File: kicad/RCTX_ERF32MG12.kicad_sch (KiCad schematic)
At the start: 93 parts, among them J20 USB_OTG, P10 LEDs, P4 SWD, P6 SD Card, P9 BUZZ, SW2 RESET, U10 ATSAMD11D14A-M, U11 USB6B1

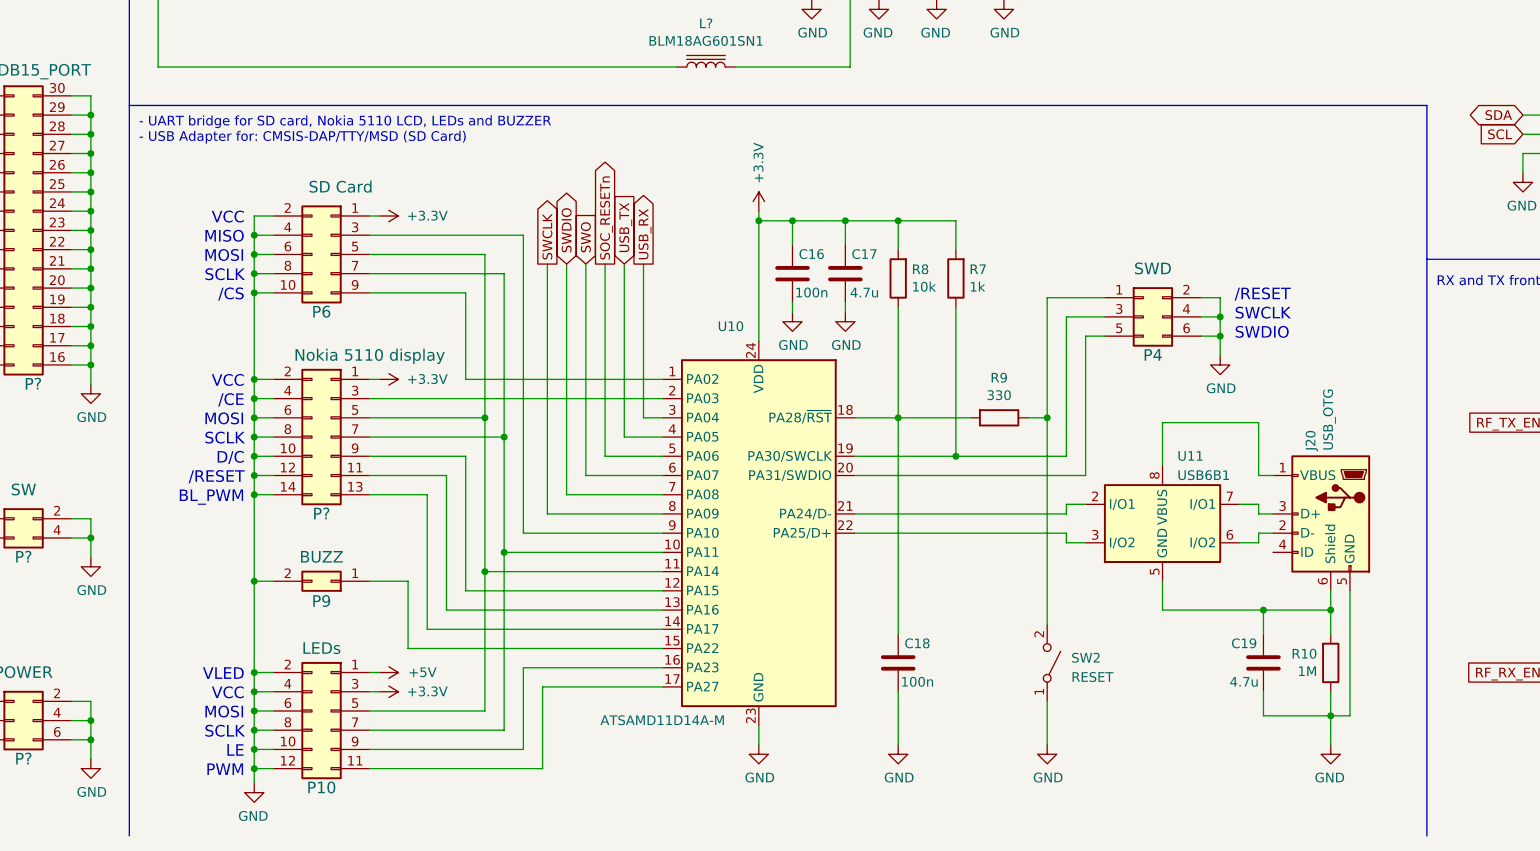
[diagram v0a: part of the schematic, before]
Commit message: Using SAMD11D14M instead of PIC16F1459 for USB bridge - updating schematics
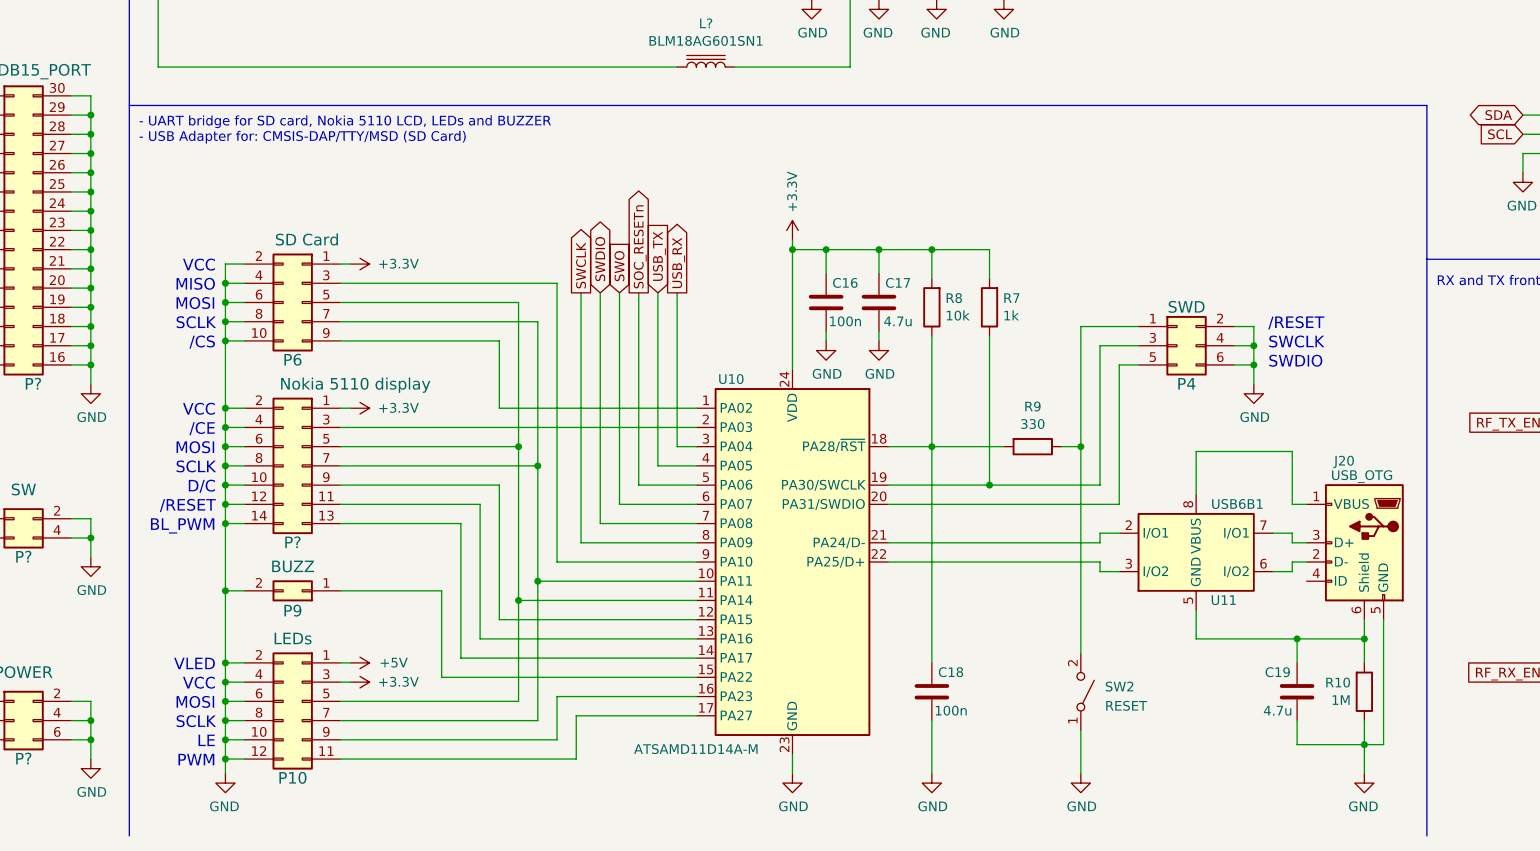
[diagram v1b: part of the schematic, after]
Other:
- moved on the sheet: C16, C17, C18, C19, J20, P10, P4, P6, P9, P?, R10, R7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

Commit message: Using SAMD11D14M instead of PIC16F1459 for USB bridge - updating schematics
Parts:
- removed C? (x6): 100p, symbol device:C
- removed P4: SWD, symbol conn:Conn_02x03_Odd_Even
- removed R8: 10k, symbol device:R
- removed R9: 330, symbol device:R
- removed SW2: RESET, symbol RCTX-rescue:SW_SPST-switches
- removed U? (x2): MAX2650, smd-semi:SOT-143, symbol RCTX_ERF32MG12-rescue:MAX2650-maxim_1
- added C1, C2, C20, C21, C22: 100p, symbol device:C
- added J21, J22: USB, symbol Connector_Generic:Conn_01x03
- added P?: AUX_DB9_PORT, symbol Connector_Generic:Conn_02x09_Odd_Even
- added U1, U12: MAX2650, smd-semi:SOT-143, symbol maxim_1:MAX2650
- C18: value 100n -> 100p
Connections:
- net +3V3: now also P?.3 (Pin_3)
- net +5V: now also P?.1 (Pin_1)
- net GND: now also C18.2, C20.2, J21.3 (Pin_3), J22.3 (Pin_3), P?.10 (Pin_10), P?.12 (Pin_12), P?.14 (Pin_14), P?.16 (Pin_16), P?.18 (Pin_18), P?.2 (Pin_2), P?.4 (Pin_4), P?.6 (Pin_6), P?.8 (Pin_8), U1.4 (VCC), U12.2 (GND); no longer C18.1
- net RF_RX_VCC: now also C20.1, U12.4 (VCC)
- net RF_TX_VCC: now also C18.1, U1.2 (GND)
- net SOC_RESETn: now also P?.5 (Pin_5)
- net at U?.8 (RF), U?.8 (RF): now also C21.2, C22.1
- net at U?.3 (RF1): now also C1.1, C2.2
- net at U11.2 (I/O1): now also J22.1 (Pin_1); no longer U10.21 (PA24/D-)
- net at U11.3 (I/O2): now also J22.2 (Pin_2); no longer U10.22 (PA25/D+)
- net DAP_SWCLK: now reaches R7.1, U10.19 (PA30/SWCLK)
- net DAP_SWCLK: now also P?.15 (Pin_15)
- net DAP_SWDIO: now reaches U10.20 (PA31/SWDIO)
- net DAP_SWDIO: now also P?.13 (Pin_13)
- net DAP_RESETn: now reaches U10.18 (PA28/~{RST})
- net DAP_RESETn: now also P?.17 (Pin_17); no longer C18.2
- net SWCLK renamed SOC_SWCLK
- net SOC_SWCLK: now also P?.11 (Pin_11)
- net SWDIO renamed SOC_SWDIO
- net SOC_SWDIO: now also P?.9 (Pin_9)
- net SWO renamed SOC_SWO
- net SOC_SWO: now also P?.7 (Pin_7)
- new net: C22.2, U12.1 (OUT)
- new net: C2.1, U12.3 (IN)
- new net: C21.1, U1.3 (IN)
- new net: J21.1 (Pin_1), U10.21 (PA24/D-)
- new net: J21.2 (Pin_2), U10.22 (PA25/D+)
- new net: C1.2, U1.1 (OUT)
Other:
- note added: "- Micro USB connector"
- note added: "HF/VHF band filter"
- note added: "Sub-GHz multiband 110 MHz up-down converter, pre-amp and power-amp RF MHz ± LO MHz -> IF MHz ------------------------ 10 ... 80 + 110 -> 120-190 430 ... 460 - 110 -> 320-350"
- note added: "UHF band filter"
- note removed: "110 MHz"
- note removed: "SWCLK"
- note removed: "SWDIO"
- moved on the sheet: C16, C17, C19, C?, J20, J?, L?, P10, P6, P9, P?, R10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

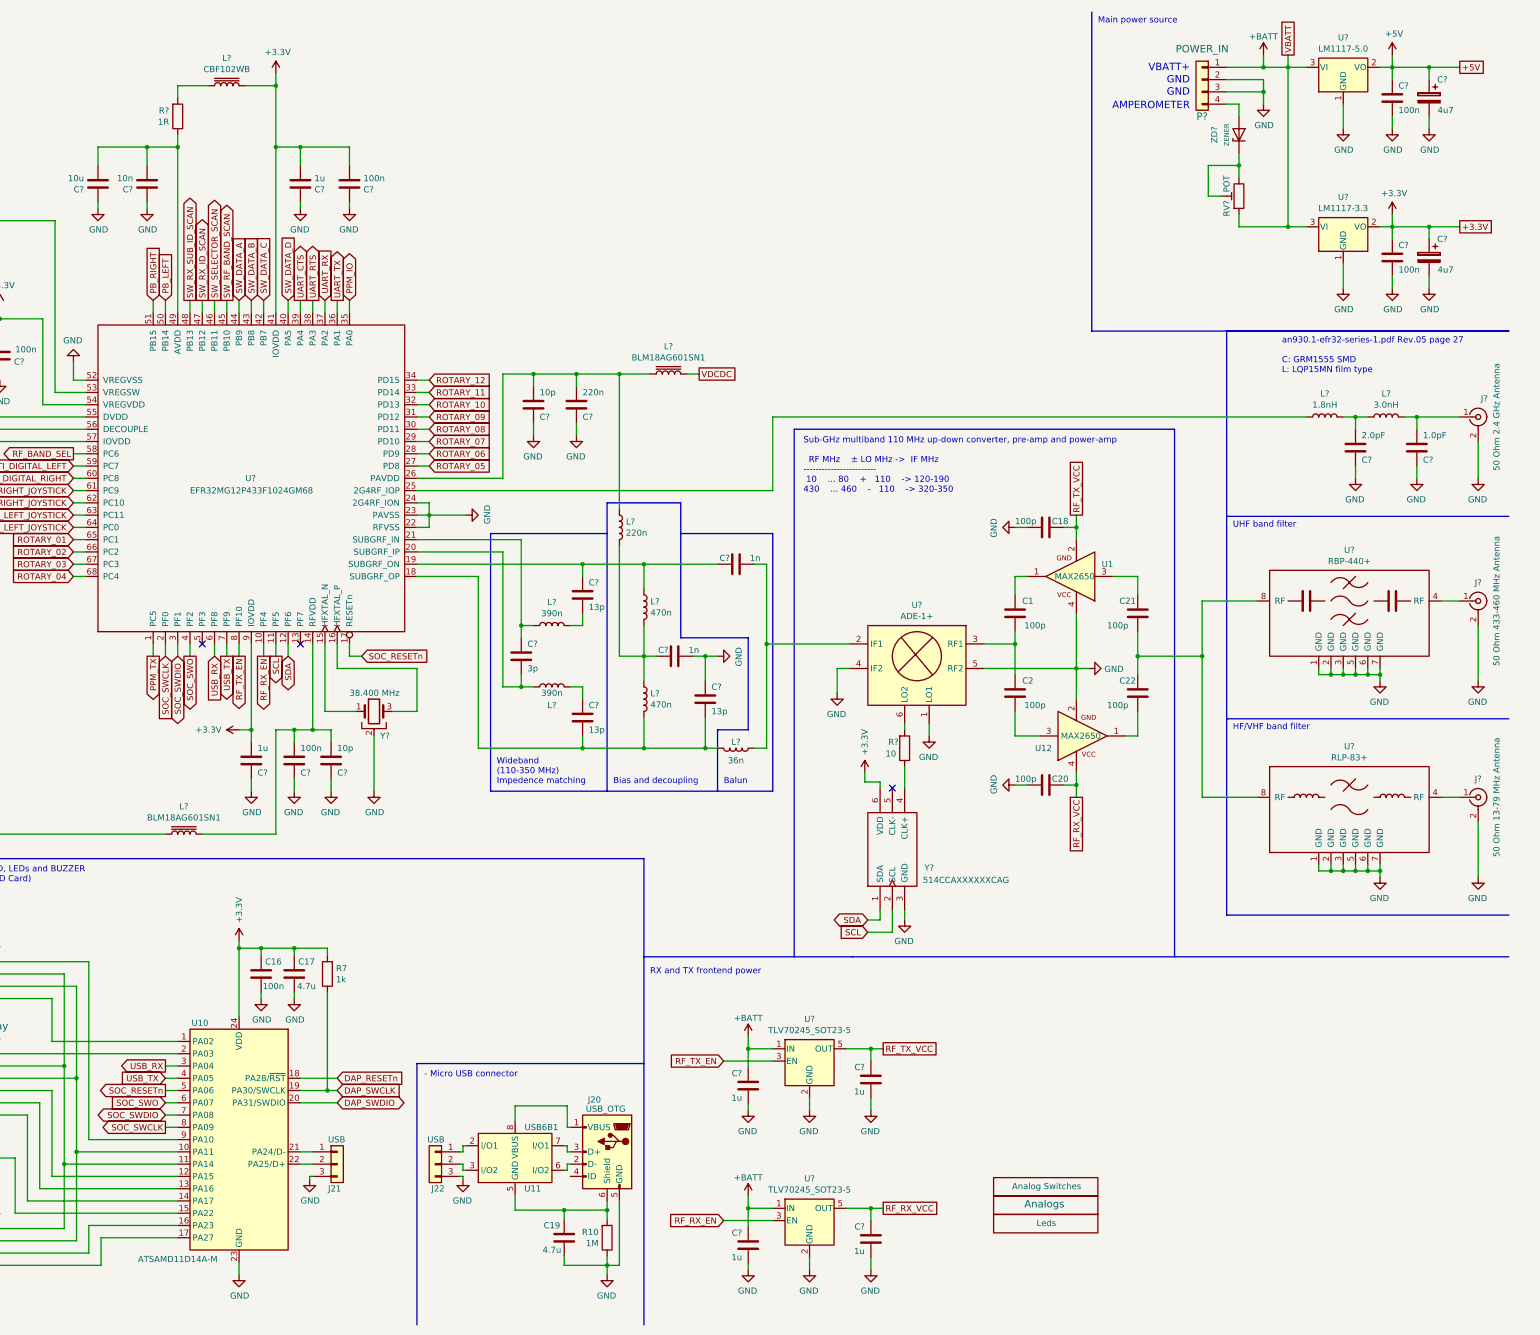
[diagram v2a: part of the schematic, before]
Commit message: Driving the EFR32 reset with the SAMD11 reset pin as GPIO to have an additional GPIO for the SPI {EFR32<->SAMD11} CLK
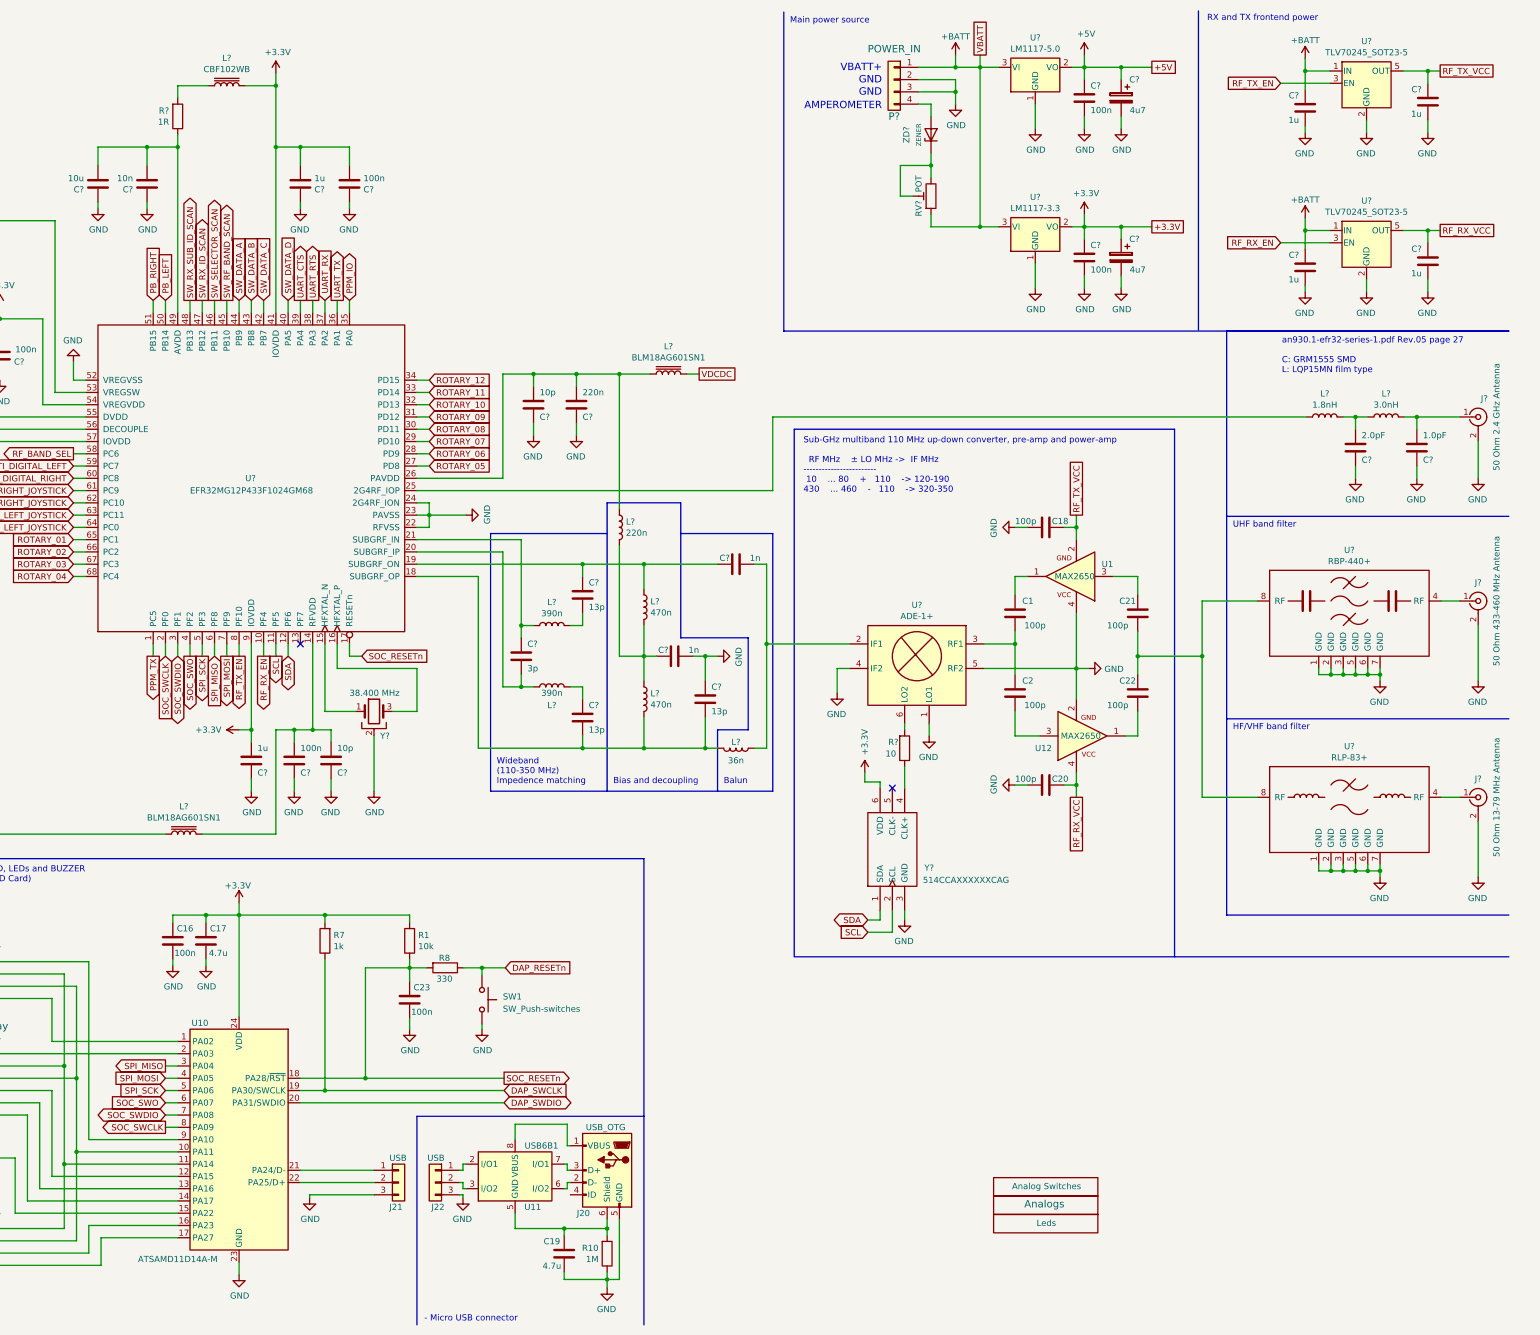
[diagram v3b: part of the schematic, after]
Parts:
- added C23: 100n, symbol device:C
- added R1: 10k, symbol device:R
- added R8: 330, symbol device:R
- added SW1: SW_Push-switches, symbol RCTX-rescue:SW_Push-switches
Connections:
- net +3V3: now also R1.2
- net DAP_RESETn: now also R8.1, SW1.2; no longer U10.18 (PA28/~{RST})
- net GND: now also C23.1, SW1.1
- net SOC_RESETn: now also U10.18 (PA28/~{RST}), C23.2, R1.1, R8.2; no longer U10.5 (PA06)
- net SPI_SCK: now reaches U?.5 (PF3)
- net SPI_SCK: now also U10.5 (PA06)
- net USB_RX renamed SPI_MISO
- net USB_TX renamed SPI_MOSI
- no-connect marks 3 -> 2
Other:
- moved on the sheet: C16, C17, C19, C?, J20, J21, J22, P?, R10, R7, RV?, U11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
